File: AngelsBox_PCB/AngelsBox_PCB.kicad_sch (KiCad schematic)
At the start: 19 parts

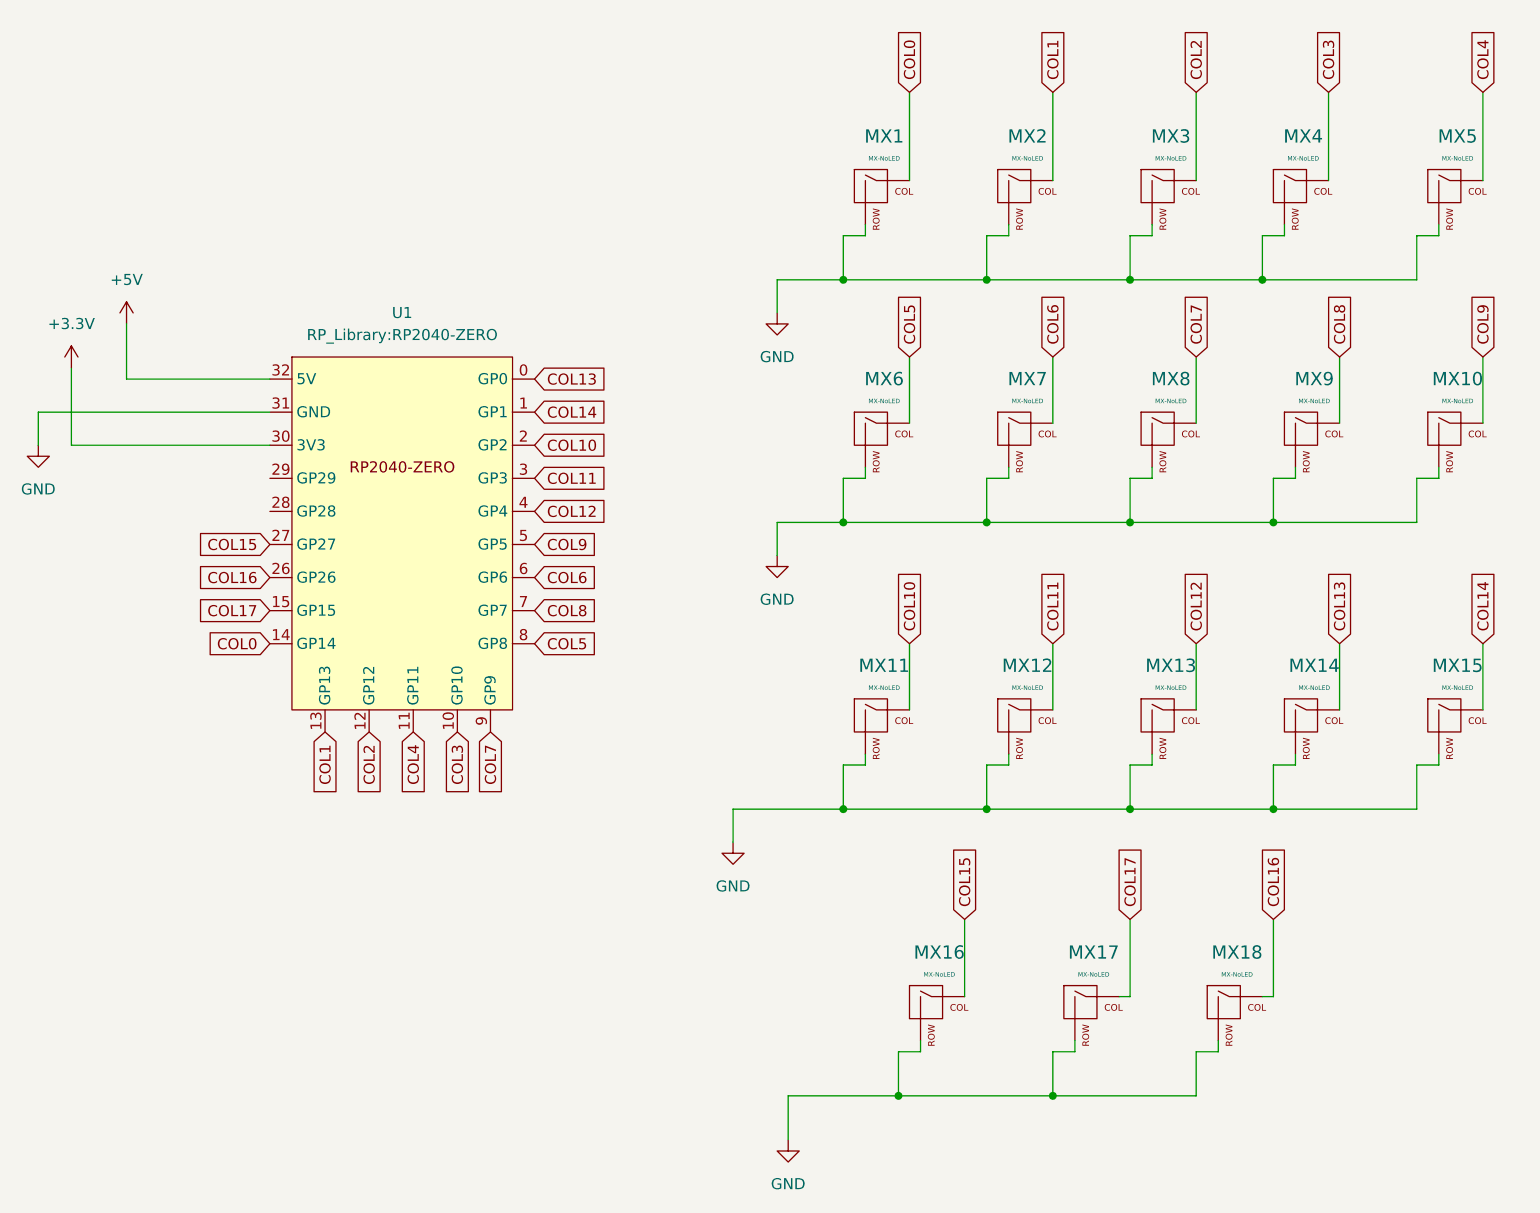
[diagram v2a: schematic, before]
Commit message: Adding small updates and a dome key cap
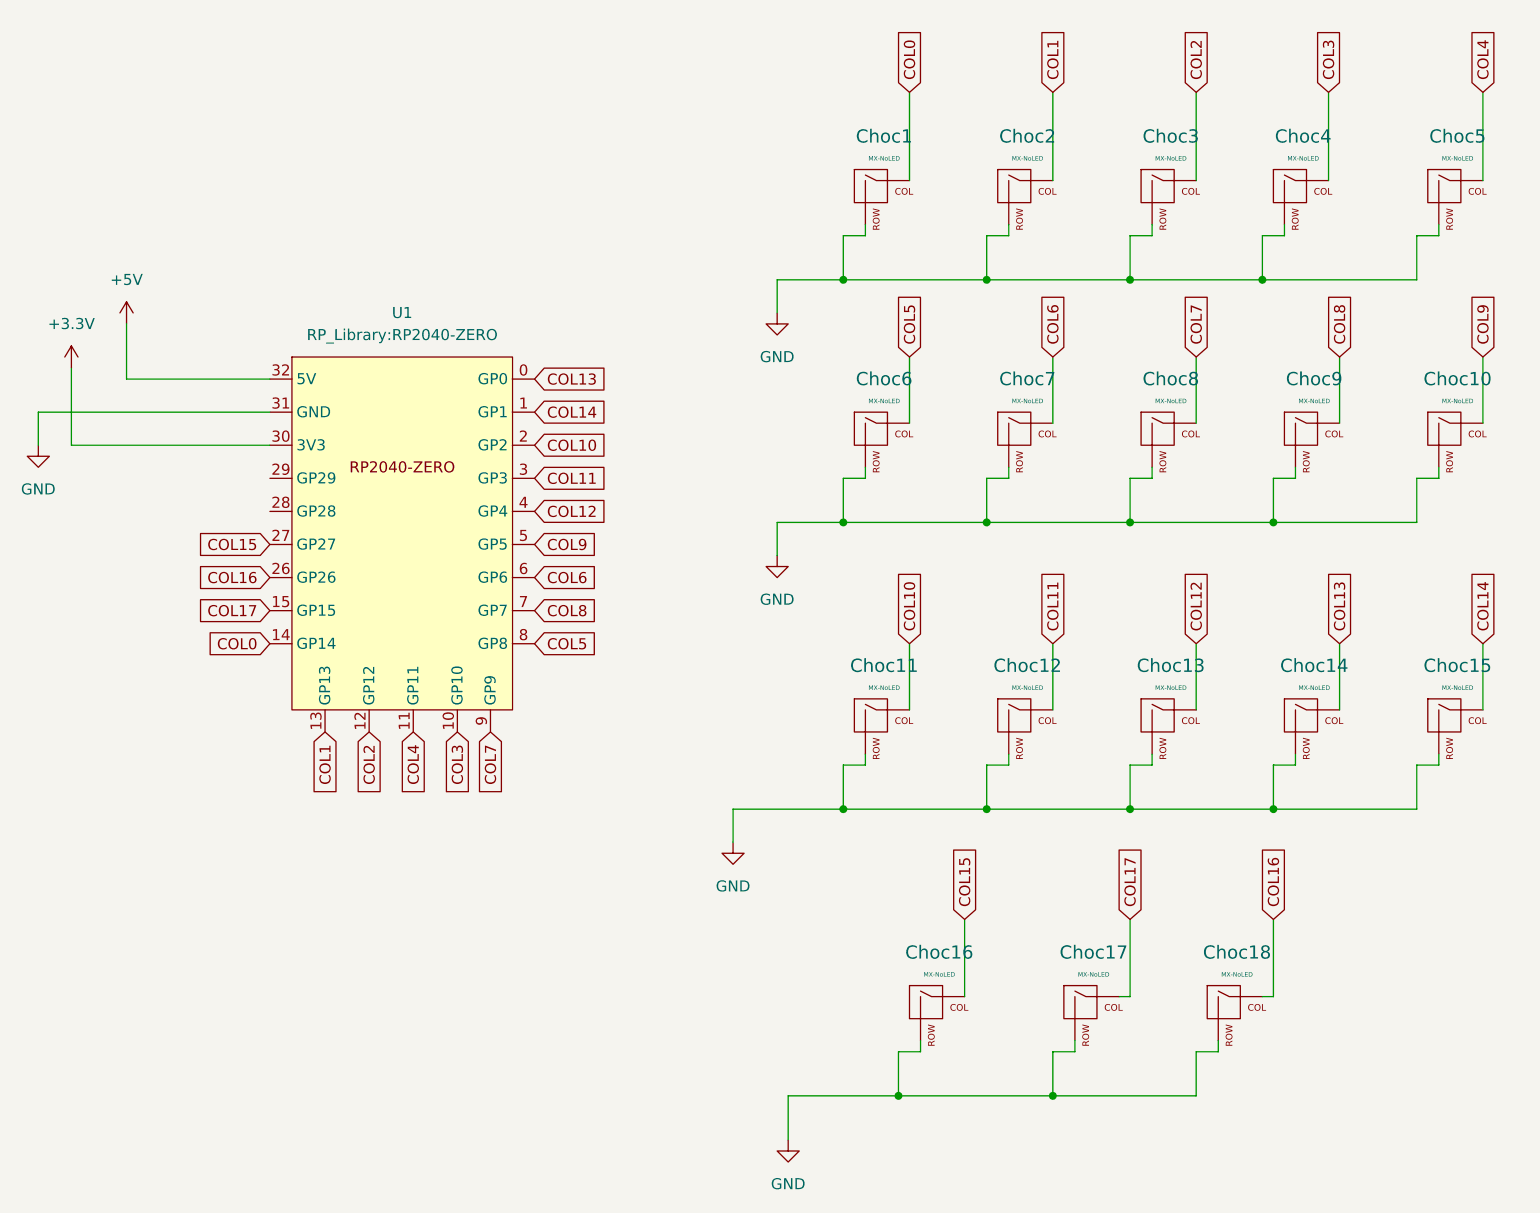
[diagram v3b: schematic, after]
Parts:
- renumbered MX1 to Choc1, MX10 to Choc10, MX11 to Choc11, MX12 to Choc12, MX13 to Choc13, MX14 to Choc14, MX15 to Choc15, MX16 to Choc16, MX17 to Choc17, MX18 to Choc18, MX2 to Choc2, MX3 to Choc3, MX4 to Choc4, MX5 to Choc5, MX6 to Choc6, MX7 to Choc7, MX8 to Choc8, MX9 to Choc9
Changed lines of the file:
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@@
   (symbol (lib_id "MX_Alps_Hybrid:MX-NoLED") (at 132.08 81.28 0) (unit 1)
     (in_bom yes) (on_board yes) (dnp no) (fields_autoplaced)
-    (property "Reference" "MX6" (at 132.9752 74.93 0)
+    (property "Reference" "Choc6" (at 132.9752 74.93 0)
       (effects (font (size 1.524 1.524)))
     )
@@
       (project "AngelsBox_PCB"
         (path "/17a0a7e4-b1bf-448f-a062-fa3a221009b9"
-          (reference "MX6") (unit 1)
+          (reference "Choc6") (unit 1)
         )
       )
@@
   (symbol (lib_id "MX_Alps_Hybrid:MX-NoLED") (at 138.43 147.32 0) (unit 1)
     (in_bom yes) (on_board yes) (dnp no) (fields_autoplaced)
-    (property "Reference" "MX16" (at 139.3252 140.97 0)
+    (property "Reference" "Choc16" (at 139.3252 140.97 0)
       (effects (font (size 1.524 1.524)))
     )
@@
       (project "AngelsBox_PCB"
         (path "/17a0a7e4-b1bf-448f-a062-fa3a221009b9"
-          (reference "MX16") (unit 1)
+          (reference "Choc16") (unit 1)
         )
       )
@@
   (symbol (lib_id "MX_Alps_Hybrid:MX-NoLED") (at 198.12 114.3 0) (unit 1)
     (in_bom yes) (on_board yes) (dnp no) (fields_autoplaced)
-    (property "Reference" "MX15" (at 199.0152 107.95 0)
+    (property "Reference" "Choc15" (at 199.0152 107.95 0)
       (effects (font (size 1.524 1.524)))
     )
@@
       (project "AngelsBox_PCB"
         (path "/17a0a7e4-b1bf-448f-a062-fa3a221009b9"
-          (reference "MX15") (unit 1)
+          (reference "Choc15") (unit 1)
         )
       )
@@
   (symbol (lib_id "MX_Alps_Hybrid:MX-NoLED") (at 148.59 114.3 0) (unit 1)
     (in_bom yes) (on_board yes) (dnp no) (fields_autoplaced)
-    (property "Reference" "MX12" (at 149.4852 107.95 0)
+    (property "Reference" "Choc12" (at 149.4852 107.95 0)
       (effects (font (size 1.524 1.524)))
     )
@@
       (project "AngelsBox_PCB"
         (path "/17a0a7e4-b1bf-448f-a062-fa3a221009b9"
-          (reference "MX12") (unit 1)
+          (reference "Choc12") (unit 1)
         )
       )
@@
   (symbol (lib_id "MX_Alps_Hybrid:MX-NoLED") (at 181.61 114.3 0) (unit 1)
     (in_bom yes) (on_board yes) (dnp no) (fields_autoplaced)
-    (property "Reference" "MX14" (at 182.5052 107.95 0)
+    (property "Reference" "Choc14" (at 182.5052 107.95 0)
       (effects (font (size 1.524 1.524)))
     )
@@
       (project "AngelsBox_PCB"
         (path "/17a0a7e4-b1bf-448f-a062-fa3a221009b9"
-          (reference "MX14") (unit 1)
+          (reference "Choc14") (unit 1)
         )
       )
@@
   (symbol (lib_id "MX_Alps_Hybrid:MX-NoLED") (at 132.08 114.3 0) (unit 1)
     (in_bom yes) (on_board yes) (dnp no) (fields_autoplaced)
-    (property "Reference" "MX11" (at 132.9752 107.95 0)
+    (property "Reference" "Choc11" (at 132.9752 107.95 0)
       (effects (font (size 1.524 1.524)))
     )
@@
       (project "AngelsBox_PCB"
         (path "/17a0a7e4-b1bf-448f-a062-fa3a221009b9"
-          (reference "MX11") (unit 1)
+          (reference "Choc11") (unit 1)
         )
       )
@@
   (symbol (lib_id "MX_Alps_Hybrid:MX-NoLED") (at 165.1 53.34 0) (unit 1)
     (in_bom yes) (on_board yes) (dnp no) (fields_autoplaced)
-    (property "Reference" "MX3" (at 165.9952 46.99 0)
+    (property "Reference" "Choc3" (at 165.9952 46.99 0)
       (effects (font (size 1.524 1.524)))
     )
@@
       (project "AngelsBox_PCB"
         (path "/17a0a7e4-b1bf-448f-a062-fa3a221009b9"
-          (reference "MX3") (unit 1)
+          (reference "Choc3") (unit 1)
         )
       )
@@
   (symbol (lib_id "MX_Alps_Hybrid:MX-NoLED") (at 148.59 53.34 0) (unit 1)
     (in_bom yes) (on_board yes) (dnp no) (fields_autoplaced)
-    (property "Reference" "MX2" (at 149.4852 46.99 0)
+    (property "Reference" "Choc2" (at 149.4852 46.99 0)
       (effects (font (size 1.524 1.524)))
     )
@@
       (project "AngelsBox_PCB"
         (path "/17a0a7e4-b1bf-448f-a062-fa3a221009b9"
-          (reference "MX2") (unit 1)
+          (reference "Choc2") (unit 1)
         )
       )
@@
   (symbol (lib_id "MX_Alps_Hybrid:MX-NoLED") (at 165.1 114.3 0) (unit 1)
     (in_bom yes) (on_board yes) (dnp no) (fields_autoplaced)
-    (property "Reference" "MX13" (at 165.9952 107.95 0)
+    (property "Reference" "Choc13" (at 165.9952 107.95 0)
       (effects (font (size 1.524 1.524)))
     )
@@
       (project "AngelsBox_PCB"
         (path "/17a0a7e4-b1bf-448f-a062-fa3a221009b9"
-          (reference "MX13") (unit 1)
+          (reference "Choc13") (unit 1)
         )
       )
@@
   (symbol (lib_id "MX_Alps_Hybrid:MX-NoLED") (at 156.21 147.32 0) (unit 1)
     (in_bom yes) (on_board yes) (dnp no) (fields_autoplaced)
-    (property "Reference" "MX17" (at 157.1052 140.97 0)
+    (property "Reference" "Choc17" (at 157.1052 140.97 0)
       (effects (font (size 1.524 1.524)))
     )
@@
       (project "AngelsBox_PCB"
         (path "/17a0a7e4-b1bf-448f-a062-fa3a221009b9"
-          (reference "MX17") (unit 1)
+          (reference "Choc17") (unit 1)
         )
       )
@@
   )
   (symbol (lib_id "MX_Alps_Hybrid:MX-NoLED") (at 148.59 81.28 0) (unit 1)
-    (in_bom yes) (on_board yes) (dnp no)
-    (property "Reference" "MX7" (at 149.4852 74.93 0)
+    (in_bom yes) (on_board yes) (dnp no) (fields_autoplaced)
+    (property "Reference" "Choc7" (at 149.4852 74.93 0)
       (effects (font (size 1.524 1.524)))
     )
@@
       (project "AngelsBox_PCB"
         (path "/17a0a7e4-b1bf-448f-a062-fa3a221009b9"
-          (reference "MX7") (unit 1)
+          (reference "Choc7") (unit 1)
         )
       )
@@
   (symbol (lib_id "MX_Alps_Hybrid:MX-NoLED") (at 181.61 81.28 0) (unit 1)
     (in_bom yes) (on_board yes) (dnp no) (fields_autoplaced)
-    (property "Reference" "MX9" (at 182.5052 74.93 0)
+    (property "Reference" "Choc9" (at 182.5052 74.93 0)
       (effects (font (size 1.524 1.524)))
     )
@@
       (project "AngelsBox_PCB"
         (path "/17a0a7e4-b1bf-448f-a062-fa3a221009b9"
-          (reference "MX9") (unit 1)
+          (reference "Choc9") (unit 1)
         )
       )
@@
   (symbol (lib_id "MX_Alps_Hybrid:MX-NoLED") (at 172.72 147.32 0) (unit 1)
     (in_bom yes) (on_board yes) (dnp no) (fields_autoplaced)
-    (property "Reference" "MX18" (at 173.6152 140.97 0)
+    (property "Reference" "Choc18" (at 173.6152 140.97 0)
       (effects (font (size 1.524 1.524)))
     )
@@
       (project "AngelsBox_PCB"
         (path "/17a0a7e4-b1bf-448f-a062-fa3a221009b9"
-          (reference "MX18") (unit 1)
+          (reference "Choc18") (unit 1)
         )
       )
@@
   (symbol (lib_id "MX_Alps_Hybrid:MX-NoLED") (at 180.34 53.34 0) (unit 1)
     (in_bom yes) (on_board yes) (dnp no) (fields_autoplaced)
-    (property "Reference" "MX4" (at 181.2352 46.99 0)
+    (property "Reference" "Choc4" (at 181.2352 46.99 0)
       (effects (font (size 1.524 1.524)))
     )
@@
       (project "AngelsBox_PCB"
         (path "/17a0a7e4-b1bf-448f-a062-fa3a221009b9"
-          (reference "MX4") (unit 1)
+          (reference "Choc4") (unit 1)
         )
       )
@@
   (symbol (lib_id "MX_Alps_Hybrid:MX-NoLED") (at 198.12 81.28 0) (unit 1)
     (in_bom yes) (on_board yes) (dnp no) (fields_autoplaced)
-    (property "Reference" "MX10" (at 199.0152 74.93 0)
+    (property "Reference" "Choc10" (at 199.0152 74.93 0)
       (effects (font (size 1.524 1.524)))
     )
@@
       (project "AngelsBox_PCB"
         (path "/17a0a7e4-b1bf-448f-a062-fa3a221009b9"
-          (reference "MX10") (unit 1)
+          (reference "Choc10") (unit 1)
         )
       )
@@
   (symbol (lib_id "MX_Alps_Hybrid:MX-NoLED") (at 198.12 53.34 0) (unit 1)
     (in_bom yes) (on_board yes) (dnp no) (fields_autoplaced)
-    (property "Reference" "MX5" (at 199.0152 46.99 0)
+    (property "Reference" "Choc5" (at 199.0152 46.99 0)
       (effects (font (size 1.524 1.524)))
     )
@@
       (project "AngelsBox_PCB"
         (path "/17a0a7e4-b1bf-448f-a062-fa3a221009b9"
-          (reference "MX5") (unit 1)
+          (reference "Choc5") (unit 1)
         )
       )
@@
   (symbol (lib_id "MX_Alps_Hybrid:MX-NoLED") (at 132.08 53.34 0) (unit 1)
     (in_bom yes) (on_board yes) (dnp no) (fields_autoplaced)
-    (property "Reference" "MX1" (at 132.9752 46.99 0)
+    (property "Reference" "Choc1" (at 132.9752 46.99 0)
       (effects (font (size 1.524 1.524)))
     )
@@
       (project "AngelsBox_PCB"
         (path "/17a0a7e4-b1bf-448f-a062-fa3a221009b9"
-          (reference "MX1") (unit 1)
+          (reference "Choc1") (unit 1)
         )
       )
@@
   )
   (symbol (lib_id "MX_Alps_Hybrid:MX-NoLED") (at 165.1 81.28 0) (unit 1)
-    (in_bom yes) (on_board yes) (dnp no)
-    (property "Reference" "MX8" (at 165.9952 74.93 0)
+    (in_bom yes) (on_board yes) (dnp no) (fields_autoplaced)
+    (property "Reference" "Choc8" (at 165.9952 74.93 0)
       (effects (font (size 1.524 1.524)))
     )
@@
       (project "AngelsBox_PCB"
         (path "/17a0a7e4-b1bf-448f-a062-fa3a221009b9"
-          (reference "MX8") (unit 1)
-        )
-      )
+          (reference "Choc8") (unit 1)
+        )
+      )

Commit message: small change to the foot prints for the key switches to support choc v1 and v2
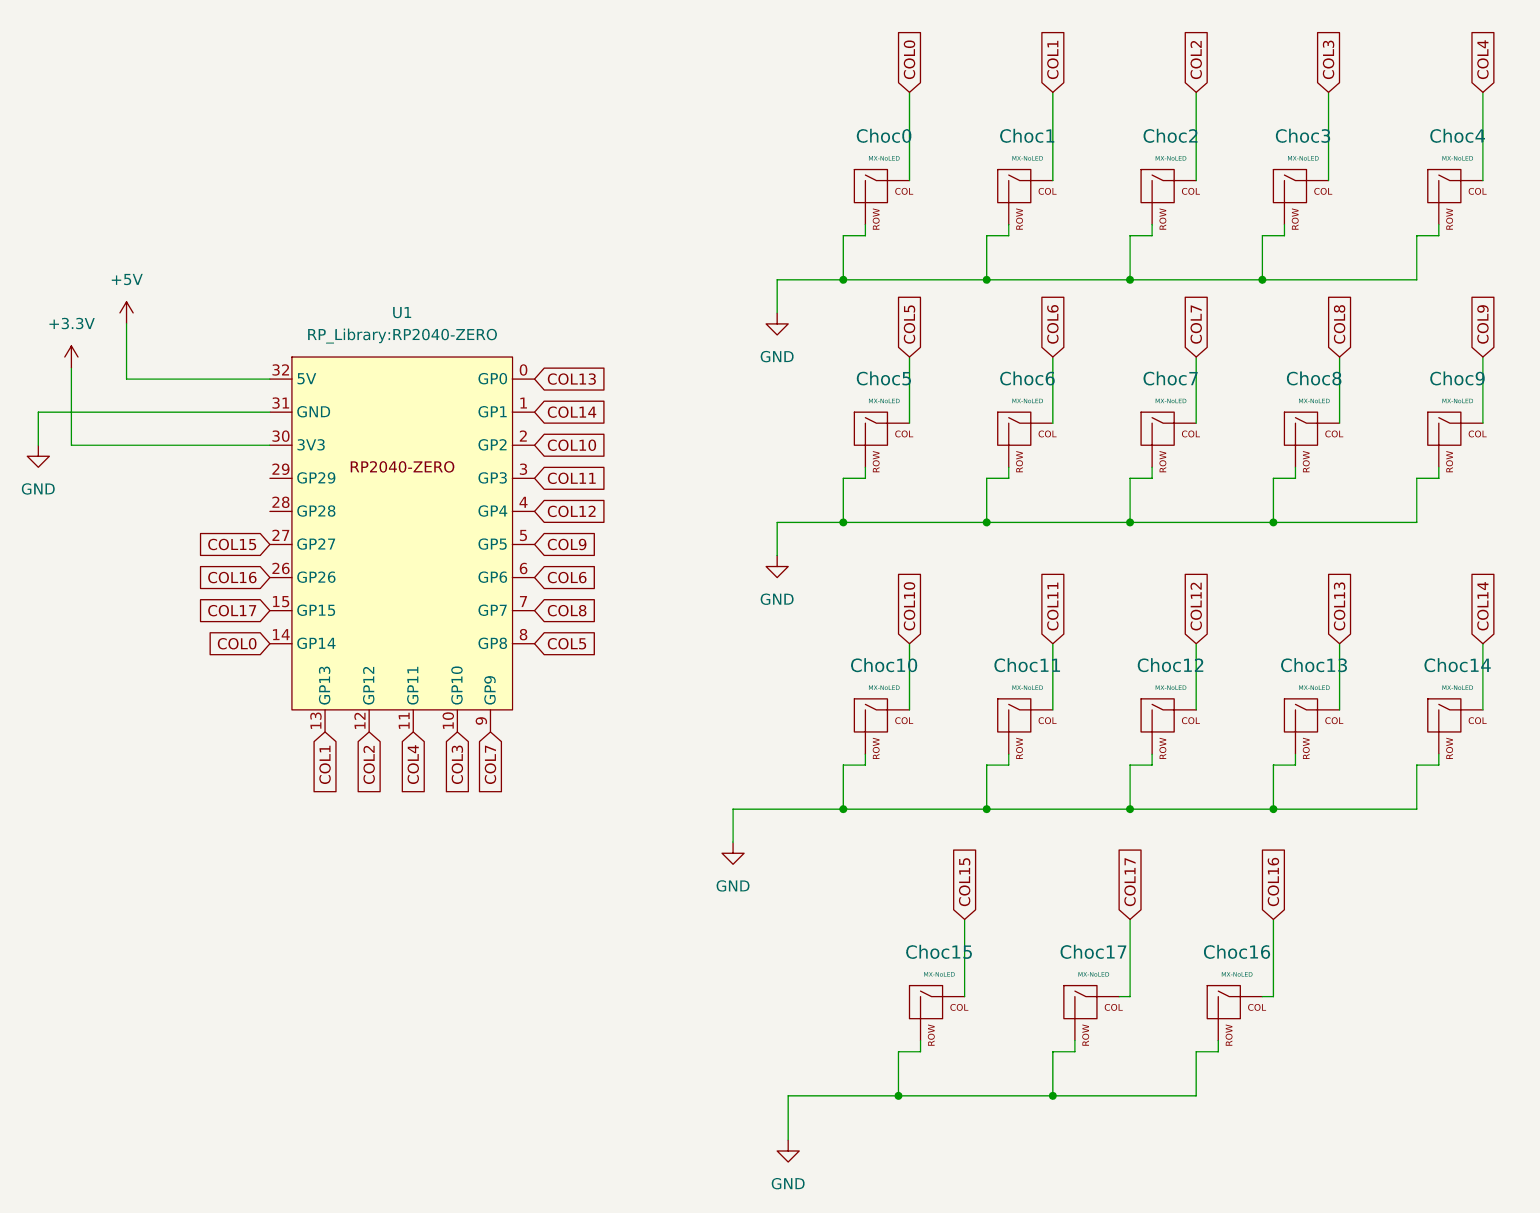
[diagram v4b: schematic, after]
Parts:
- renumbered Choc1 to Choc0, Choc2 to Choc1, Choc11 to Choc10, Choc12 to Choc11, Choc13 to Choc12, Choc14 to Choc13, Choc15 to Choc14, Choc16 to Choc15, Choc18 to Choc16, Choc3 to Choc2, Choc4 to Choc3, Choc5 to Choc4, Choc6 to Choc5, Choc7 to Choc6, Choc8 to Choc7, Choc9 to Choc8, Choc10 to Choc9
